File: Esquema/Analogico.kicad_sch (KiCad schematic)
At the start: 43 parts, among them J1 Conex_bat, J2 Panel Solar, J3 Galga_1, J4 Galga_2, P1 USB_C_Plug_USB2.0, U1 REF3020AIDBZT, U10 NUCLEO-F429ZI, U2 INA826AIDR, U3 TP4057, U4 INA826AIDR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

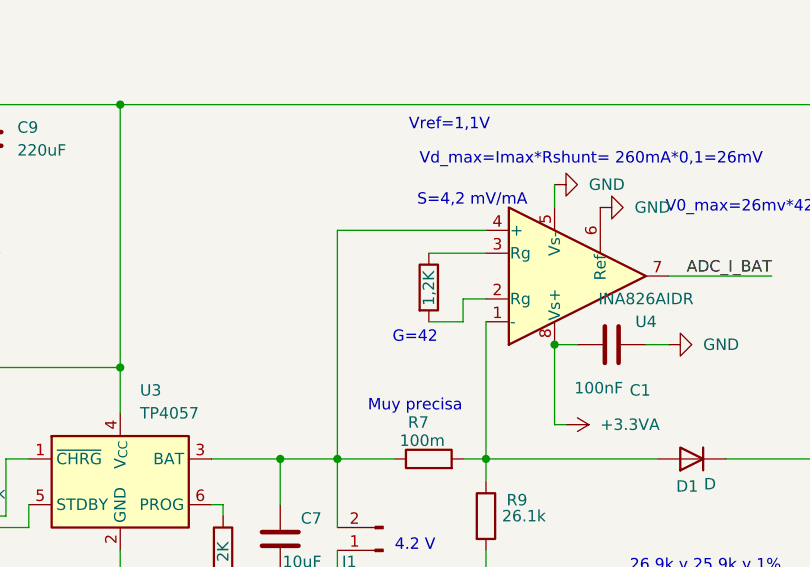
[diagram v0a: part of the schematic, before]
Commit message: añado el modo stop
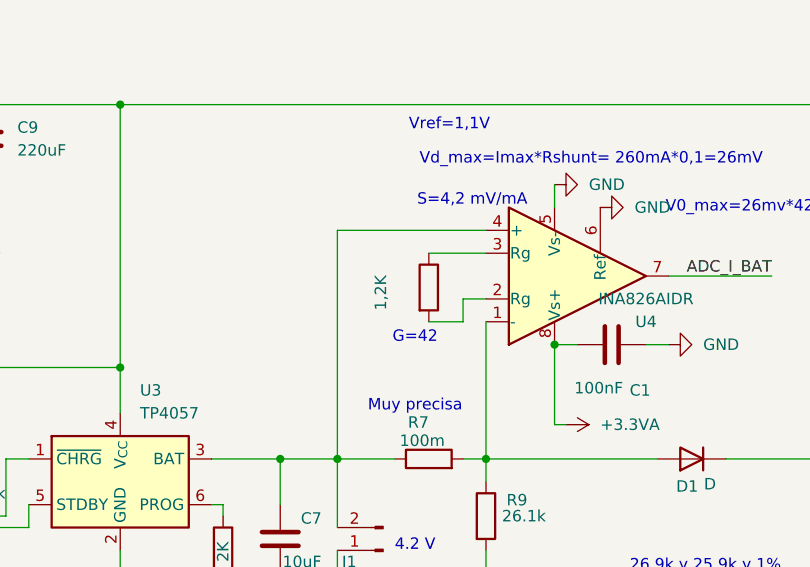
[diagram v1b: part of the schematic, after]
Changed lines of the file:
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@@
 		)
 		(property "Value" "1,2K"
-			(at 160.02 54.102 90)
+			(at 154.686 54.61 90)
 			(effects
 				(font
